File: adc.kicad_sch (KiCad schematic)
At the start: 12 parts

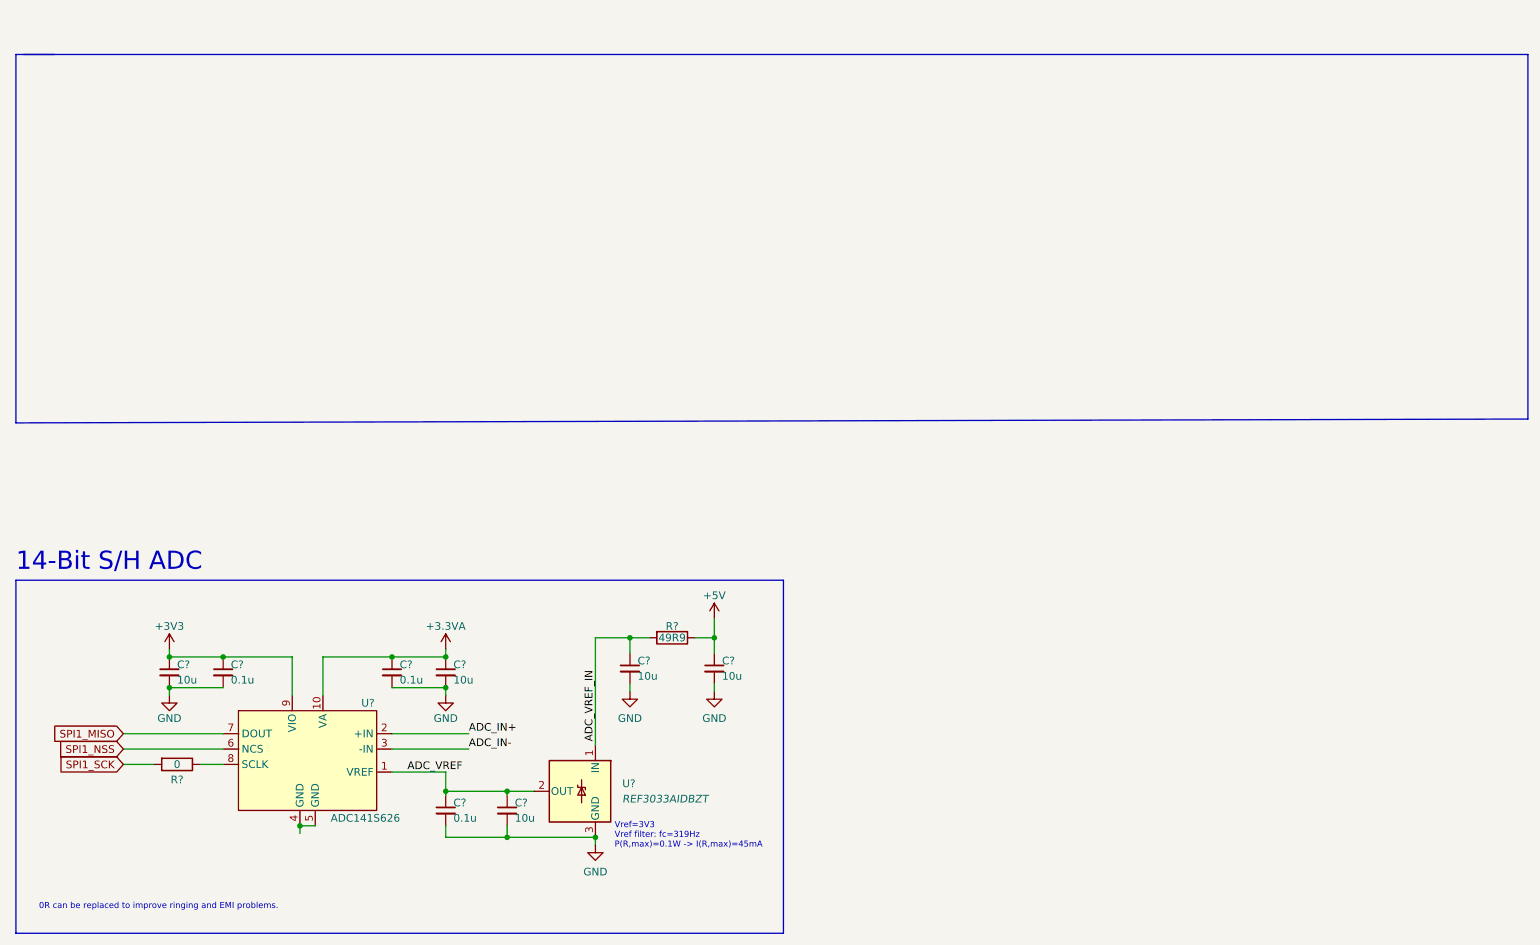
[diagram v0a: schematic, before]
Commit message: Completed ADC, DAC, Analogue In, and Analogue Out
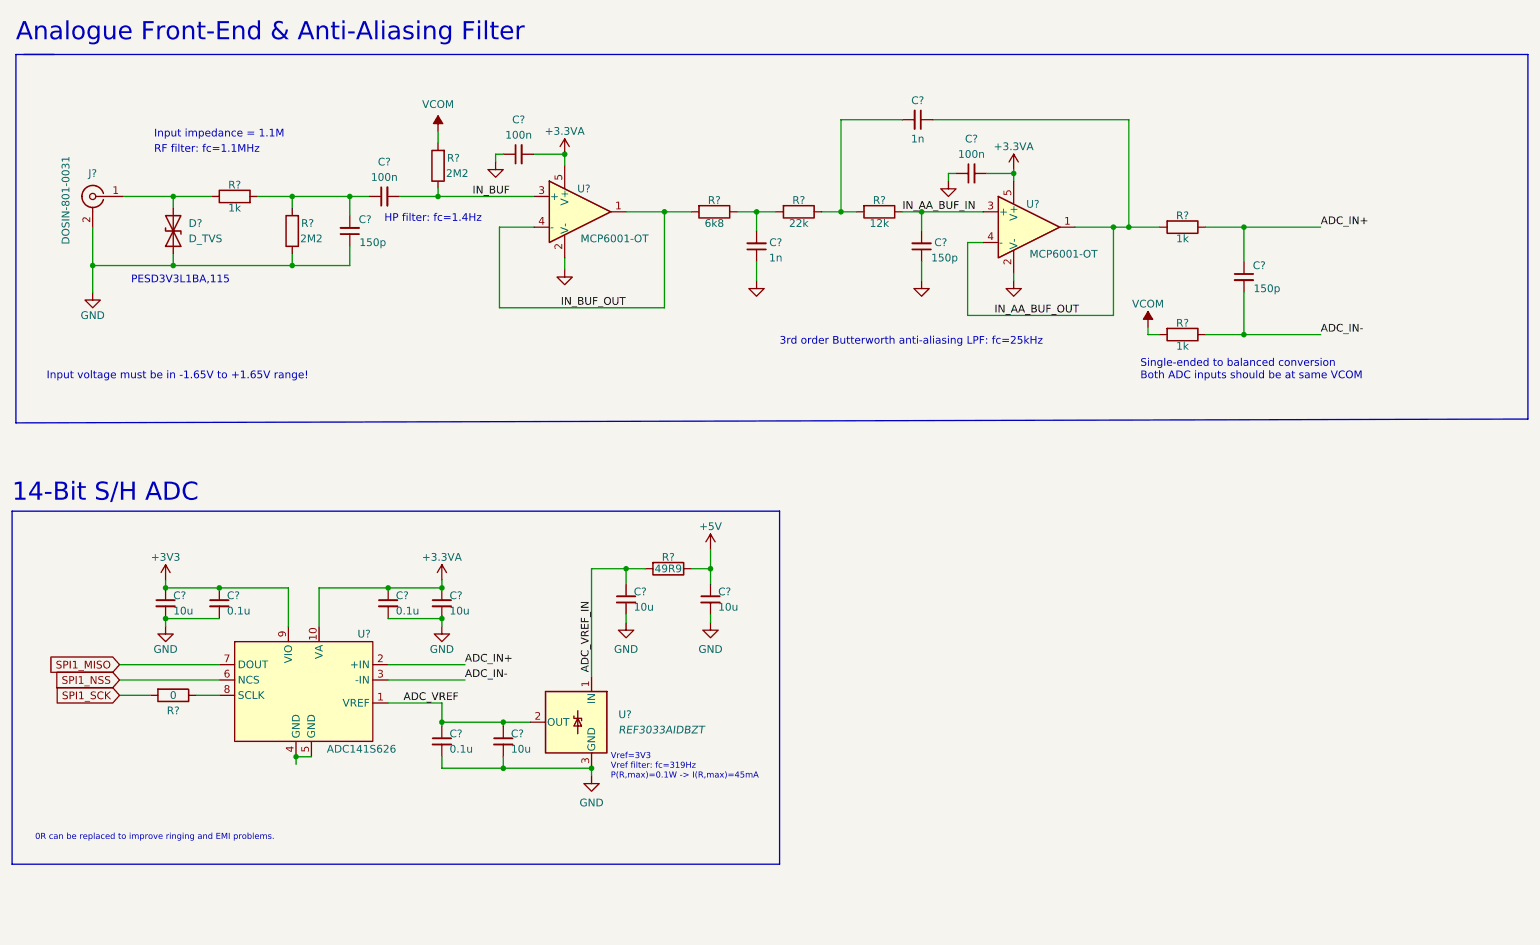
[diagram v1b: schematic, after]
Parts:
- added C? (x3): 100n, symbol Device:C_Small
- added C? (x3): 150p, symbol Device:C_Small
- added C? (x2): 1n, symbol Device:C_Small
- added D?: D_TVS, symbol Device:D_TVS
- added J?: DOSIN-801-0031, symbol Connector:Conn_Coaxial
- added R?: 12k, symbol Device:R
- added R? (x3): 1k, symbol Device:R
- added R?: 6k8, symbol Device:R
- added R? (x2): 2M2, symbol Device:R
- added R?: 22k, symbol Device:R
- added U? (x2): MCP6001-OT, Package_TO_SOT_SMD:SOT-23-5, symbol Amplifier_Operational:MCP6001-OT
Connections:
- net +3.3VA: now also C?.2, C?.2, U?.5 (V+), U?.5 (V+)
- net ADC_IN+: now also C?.1, R?.1
- net ADC_IN-: now also C?.2, R?.1
- net GND: now also C?.1, C?.1, C?.1, C?.1, C?.1, D?.1 (A1), J?.2 (Ext), R?.1, U?.2 (V-), U?.2 (V-)
- new net: C?.2, R?.1, R?.2 (x2)
- new net: D?.2 (A2), J?.1 (In), R?.1
- new net: C?.1, C?.2, R?.2, R?.2
- new net IN_AA_BUF_IN: C?.2, R?.1, U?.3 (+)
- new net IN_AA_BUF_OUT: C?.1, R?.2, U?.1, U?.4 (-)
- new net IN_BUF: C?.2, R?.1, U?.3 (+)
- new net IN_BUF_OUT: R?.2, U?.1, U?.4 (-)
- new net VCOM: R?.2, R?.2
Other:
- note added: "3rd order Butterworth anti-aliasing LPF: fc=25kHz"
- note added: "Analogue Front-End & Anti-Aliasing Filter"
- note added: "HP filter: fc=1.4Hz"
- note added: "Input impedance = 1.1M"
- note added: "Input voltage must be in -1.65V to +1.65V range!"
- note added: "PESD3V3L1BA,115"
- note added: "RF filter: fc=1.1MHz"
- note added: "Single-ended to balanced conversion Both ADC inputs should be at same VCOM"
- company: (none) -> Jonathan Podiono
- title: (none) -> ADC & Analogue In
- moved on the sheet: C?, R?, U?

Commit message: ERC valid.
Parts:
- gave numbers to parts that had none: 32
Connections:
- net GND: now also U302.4 (GND), U302.5 (GND)

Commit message: Assigned Footprints and Set up board specifications.
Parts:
- C300, C301, C302, C303, C304, C305, C306, C307, C311, C312, C314: footprint (none) -> Capacitor_SMD:C_0402_1005Metric
- C308, C309, C310, C313, C315: footprint (none) -> Capacitor_SMD:C_0603_1608Metric
- D300: footprint (none) -> Diode_SMD:D_SOD-323
- J300: footprint (none) -> Connector_Coaxial:BNC_Amphenol_031-6575_Horizontal
- R300, R301, R302, R303, R304, R305, R306, R307, R308, R309: footprint (none) -> Resistor_SMD:R_0402_1005Metric
- U302: footprint (none) -> my_footprints:SOIC-10
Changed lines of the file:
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@@
     (property "Reference" "R304" (id 0) (at 168.275 52.705 90))
     (property "Value" "12k" (id 1) (at 168.275 56.515 90))
-    (property "Footprint" "" (id 2) (at 168.275 52.832 90)
+    (property "Footprint" "Resistor_SMD:R_0402_1005Metric" (id 2) (at 168.275 52.832 90)
       (effects (font (size 1.27 1.27)) hide)
     )
@@
       (effects (font (size 1.27 1.27)) (justify left))
     )
-    (property "Footprint" "" (id 2) (at 95.885 142.24 0)
+    (property "Footprint" "Capacitor_SMD:C_0402_1005Metric" (id 2) (at 95.885 142.24 0)
       (effects (font (size 1.27 1.27)) hide)
     )
@@
     (property "Reference" "R308" (id 0) (at 133.35 111.76 90))
     (property "Value" "49R9" (id 1) (at 133.35 113.665 90))
-    (property "Footprint" "" (id 2) (at 133.35 111.887 90)
+    (property "Footprint" "Resistor_SMD:R_0402_1005Metric" (id 2) (at 133.35 111.887 90)
       (effects (font (size 1.27 1.27)) hide)
     )
@@
     (property "Reference" "R301" (id 0) (at 61.595 50.165 90))
     (property "Value" "1k" (id 1) (at 61.595 53.975 90))
-    (property "Footprint" "" (id 2) (at 61.595 53.848 90)
+    (property "Footprint" "Resistor_SMD:R_0402_1005Metric" (id 2) (at 61.595 53.848 90)
       (effects (font (size 1.27 1.27)) hide)
     )
@@
     (property "Reference" "R302" (id 0) (at 140.97 52.705 90))
     (property "Value" "6k8" (id 1) (at 140.97 56.515 90))
-    (property "Footprint" "" (id 2) (at 140.97 52.832 90)
+    (property "Footprint" "Resistor_SMD:R_0402_1005Metric" (id 2) (at 140.97 52.832 90)
       (effects (font (size 1.27 1.27)) hide)
     )
@@
     (property "Reference" "R309" (id 0) (at 51.435 137.16 90))
     (property "Value" "0" (id 1) (at 51.435 134.62 90))
-    (property "Footprint" "" (id 2) (at 51.435 132.842 90)
+    (property "Footprint" "Resistor_SMD:R_0402_1005Metric" (id 2) (at 51.435 132.842 90)
       (effects (font (size 1.27 1.27)) hide)
     )
@@
       (effects (font (size 1.27 1.27)) (justify left))
     )
-    (property "Footprint" "" (id 2) (at 86.995 119.38 0)
+    (property "Footprint" "Capacitor_SMD:C_0402_1005Metric" (id 2) (at 86.995 119.38 0)
       (effects (font (size 1.27 1.27)) hide)
     )
@@
     (property "Reference" "R300" (id 0) (at 99.06 45.72 0))
     (property "Value" "2M2" (id 1) (at 98.425 48.26 0))
-    (property "Footprint" "" (id 2) (at 97.028 46.99 90)
+    (property "Footprint" "Resistor_SMD:R_0402_1005Metric" (id 2) (at 97.028 46.99 90)
       (effects (font (size 1.27 1.27)) hide)
     )
@@
     (property "Reference" "C303" (id 0) (at 86.36 46.355 90))
     (property "Value" "100n" (id 1) (at 86.36 48.895 90))
-    (property "Footprint" "" (id 2) (at 86.36 52.07 0)
+    (property "Footprint" "Capacitor_SMD:C_0402_1005Metric" (id 2) (at 86.36 52.07 0)
       (effects (font (size 1.27 1.27)) hide)
     )
@@
     (property "Reference" "C301" (id 0) (at 108.585 39.37 90))
     (property "Value" "100n" (id 1) (at 108.585 41.91 90))
-    (property "Footprint" "" (id 2) (at 108.585 45.085 0)
+    (property "Footprint" "Capacitor_SMD:C_0402_1005Metric" (id 2) (at 108.585 45.085 0)
       (effects (font (size 1.27 1.27)) hide)
     )
@@
       (effects (font (size 1.27 1.27)) (justify left))
     )
-    (property "Footprint" "" (id 2) (at 50.165 119.38 0)
+    (property "Footprint" "Capacitor_SMD:C_0603_1608Metric" (id 2) (at 50.165 119.38 0)
       (effects (font (size 1.27 1.27)) hide)
     )
@@
     (property "Reference" "C306" (id 0) (at 178.435 58.42 0))
     (property "Value" "150p" (id 1) (at 178.435 62.23 0))
-    (property "Footprint" "" (id 2) (at 175.26 60.325 0)
+    (property "Footprint" "Capacitor_SMD:C_0402_1005Metric" (id 2) (at 175.26 60.325 0)
       (effects (font (size 1.27 1.27)) hide)
     )
@@
     (property "Reference" "R306" (id 0) (at 74.93 56.515 0))
     (property "Value" "2M2" (id 1) (at 74.295 59.055 0))
-    (property "Footprint" "" (id 2) (at 72.898 57.785 90)
+    (property "Footprint" "Resistor_SMD:R_0402_1005Metric" (id 2) (at 72.898 57.785 90)
       (effects (font (size 1.27 1.27)) hide)
     )
@@
       (effects (font (size 1.27 1.27)) (justify left))
     )
-    (property "Footprint" "" (id 2) (at 75.565 153.67 0)
+    (property "Footprint" "my_footprints:SOIC-10" (id 2) (at 75.565 153.67 0)
       (effects (font (size 1.27 1.27)) hide)
     )
@@
       (effects (font (size 1.27 1.27)) (justify left))
     )
-    (property "Footprint" "" (id 2) (at 140.335 118.745 0)
+    (property "Footprint" "Capacitor_SMD:C_0603_1608Metric" (id 2) (at 140.335 118.745 0)
       (effects (font (size 1.27 1.27)) hide)
     )
@@
     (property "Reference" "R307" (id 0) (at 218.44 73.025 90))
     (property "Value" "1k" (id 1) (at 218.44 76.835 90))
-    (property "Footprint" "" (id 2) (at 218.44 73.152 90)
+    (property "Footprint" "Resistor_SMD:R_0402_1005Metric" (id 2) (at 218.44 73.152 90)
       (effects (font (size 1.27 1.27)) hide)
     )
@@
     (property "Reference" "R305" (id 0) (at 218.44 55.245 90))
     (property "Value" "1k" (id 1) (at 218.44 59.055 90))
-    (property "Footprint" "" (id 2) (at 218.44 55.372 90)
+    (property "Footprint" "Resistor_SMD:R_0402_1005Metric" (id 2) (at 218.44 55.372 90)
       (effects (font (size 1.27 1.27)) hide)
     )
@@
       (effects (font (size 1.27 1.27)) (justify left))
     )
-    (property "Footprint" "" (id 2) (at 126.365 118.745 0)
+    (property "Footprint" "Capacitor_SMD:C_0603_1608Metric" (id 2) (at 126.365 118.745 0)
       (effects (font (size 1.27 1.27)) hide)
     )
@@
     (property "Reference" "J300" (id 0) (at 38.1 48.26 0))
     (property "Value" "DOSIN-801-0031" (id 1) (at 33.655 52.705 90))
-    (property "Footprint" "" (id 2) (at 38.1 52.07 0)
+    (property "Footprint" "Connector_Coaxial:BNC_Amphenol_031-6575_Horizontal" (id 2) (at 38.1 52.07 0)
       (effects (font (size 1.27 1.27)) hide)
     )
@@
       (effects (font (size 1.27 1.27)) (justify left))
     )
-    (property "Footprint" "" (id 2) (at 59.055 119.38 0)
+    (property "Footprint" "Capacitor_SMD:C_0402_1005Metric" (id 2) (at 59.055 119.38 0)
       (effects (font (size 1.27 1.27)) hide)
     )
@@
     (property "Reference" "C302" (id 0) (at 183.515 42.545 90))
     (property "Value" "100n" (id 1) (at 183.515 45.085 90))
-    (property "Footprint" "" (id 2) (at 183.515 48.26 0)
+    (property "Footprint" "Capacitor_SMD:C_0402_1005Metric" (id 2) (at 183.515 48.26 0)
       (effects (font (size 1.27 1.27)) hide)
     )
@@
       (effects (font (size 1.27 1.27)) (justify right))
     )
-    (property "Footprint" "" (id 2) (at 51.435 57.785 0)
+    (property "Footprint" "Diode_SMD:D_SOD-323" (id 2) (at 51.435 57.785 0)
       (effects (font (size 1.27 1.27)) hide)
     )
@@
     (property "Reference" "C307" (id 0) (at 231.14 63.5 0))
     (property "Value" "150p" (id 1) (at 232.41 67.31 0))
-    (property "Footprint" "" (id 2) (at 228.6 65.405 0)
+    (property "Footprint" "Capacitor_SMD:C_0402_1005Metric" (id 2) (at 228.6 65.405 0)
       (effects (font (size 1.27 1.27)) hide)
     )
@@
     (property "Reference" "C300" (id 0) (at 174.625 36.195 90))
     (property "Value" "1n" (id 1) (at 174.625 42.545 90))
-    (property "Footprint" "" (id 2) (at 174.625 39.37 0)
+    (property "Footprint" "Capacitor_SMD:C_0402_1005Metric" (id 2) (at 174.625 39.37 0)
       (effects (font (size 1.27 1.27)) hide)
     )
@@
     (property "Reference" "R303" (id 0) (at 154.94 52.705 90))
     (property "Value" "22k" (id 1) (at 154.94 56.515 90))
-    (property "Footprint" "" (id 2) (at 154.94 52.832 90)
+    (property "Footprint" "Resistor_SMD:R_0402_1005Metric" (id 2) (at 154.94 52.832 90)
       (effects (font (size 1.27 1.27)) hide)
     )
@@
       (effects (font (size 1.27 1.27)) (justify left))
     )
-    (property "Footprint" "" (id 2) (at 106.045 142.24 0)
+    (property "Footprint" "Capacitor_SMD:C_0603_1608Metric" (id 2) (at 106.045 142.24 0)
       (effects (font (size 1.27 1.27)) hide)
     )
@@
       (effects (font (size 1.27 1.27)) (justify left))
     )
-    (property "Footprint" "" (id 2) (at 95.885 119.38 0)
+    (property "Footprint" "Capacitor_SMD:C_0603_1608Metric" (id 2) (at 95.885 119.38 0)
       (effects (font (size 1.27 1.27)) hide)
     )
@@
     (property "Reference" "C305" (id 0) (at 151.13 58.42 0))
     (property "Value" "1n" (id 1) (at 150.495 62.23 0))
-    (property "Footprint" "" (id 2) (at 147.955 60.325 0)
+    (property "Footprint" "Capacitor_SMD:C_0402_1005Metric" (id 2) (at 147.955 60.325 0)
       (effects (font (size 1.27 1.27)) hide)
     )
@@
     (property "Reference" "C304" (id 0) (at 83.185 55.88 0))
     (property "Value" "150p" (id 1) (at 83.82 59.69 0))
-    (property "Footprint" "" (id 2) (at 80.645 57.785 0)
-      (effects (font (size 1.27 1.27)) hide)
-    )
+    (property "Footprint" "Capacitor_SMD:C_0402_1005Metric" (id 2) (at 80.645 57.785 0)
+      (effects (font (size 1.27 1.27)) hide)
+    )
